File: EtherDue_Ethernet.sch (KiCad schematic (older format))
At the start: 35 parts, among them IC601 W5100, Q601 2N7002, U601 MICROSD, U602 HY931147C, U603 APX811-44UG-7, X601 TXC 7A 25MHz 18pF

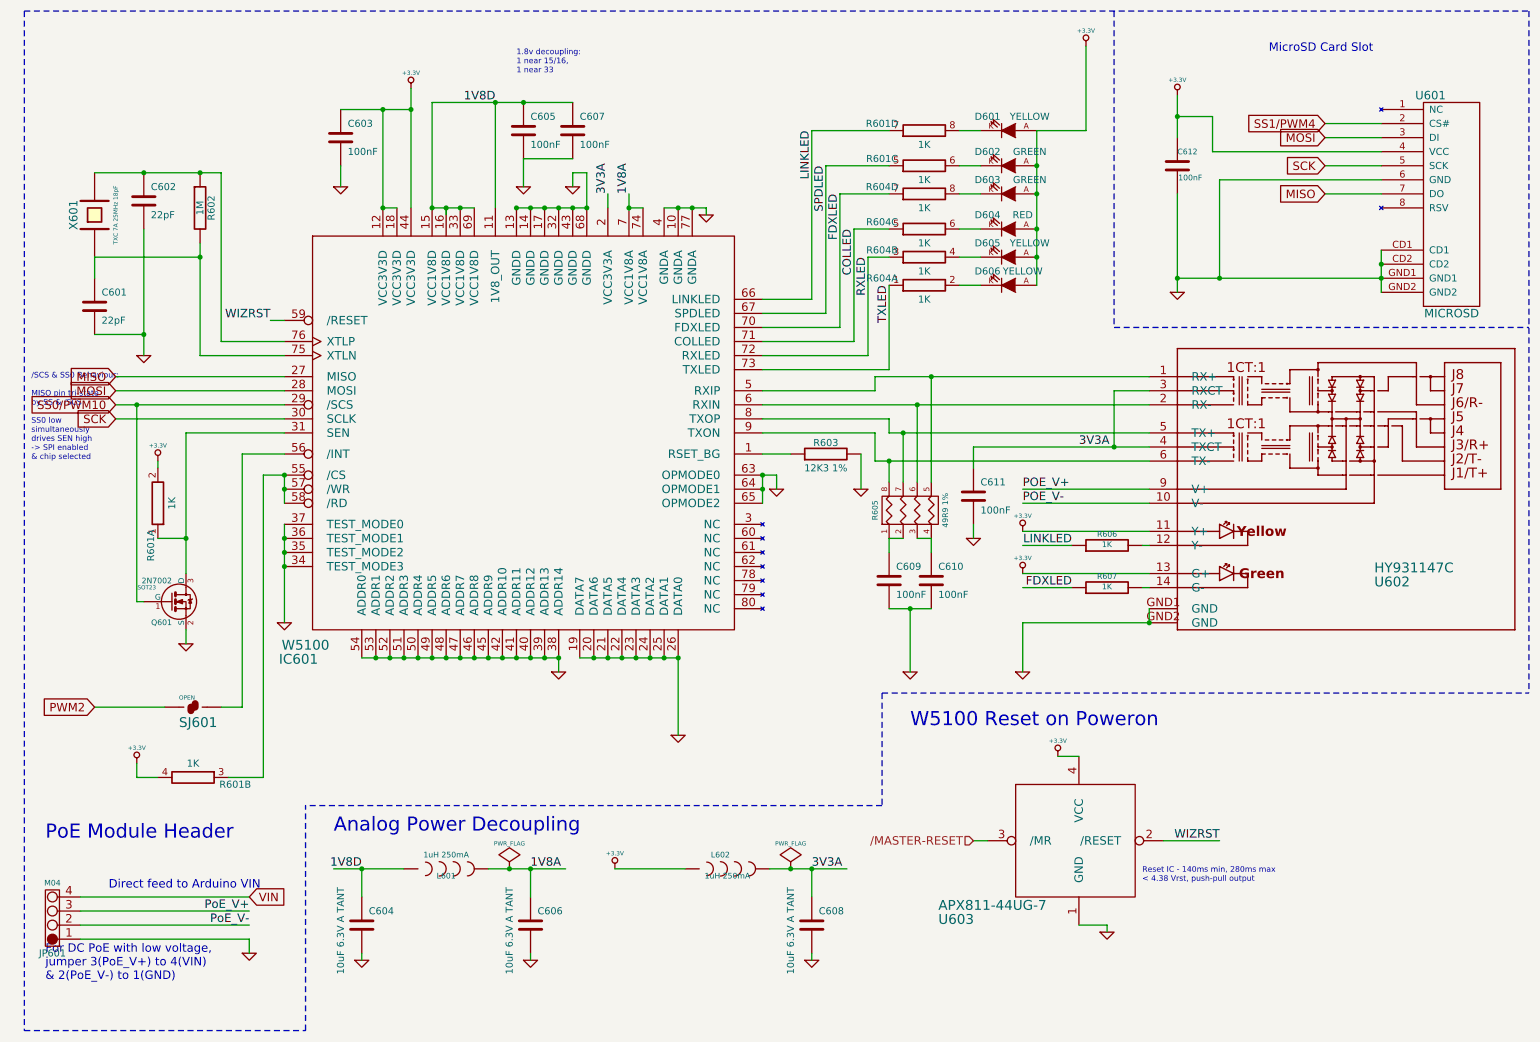
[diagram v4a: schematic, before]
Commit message: Add 24AA025E48 EEPROM w/ unique MAC address
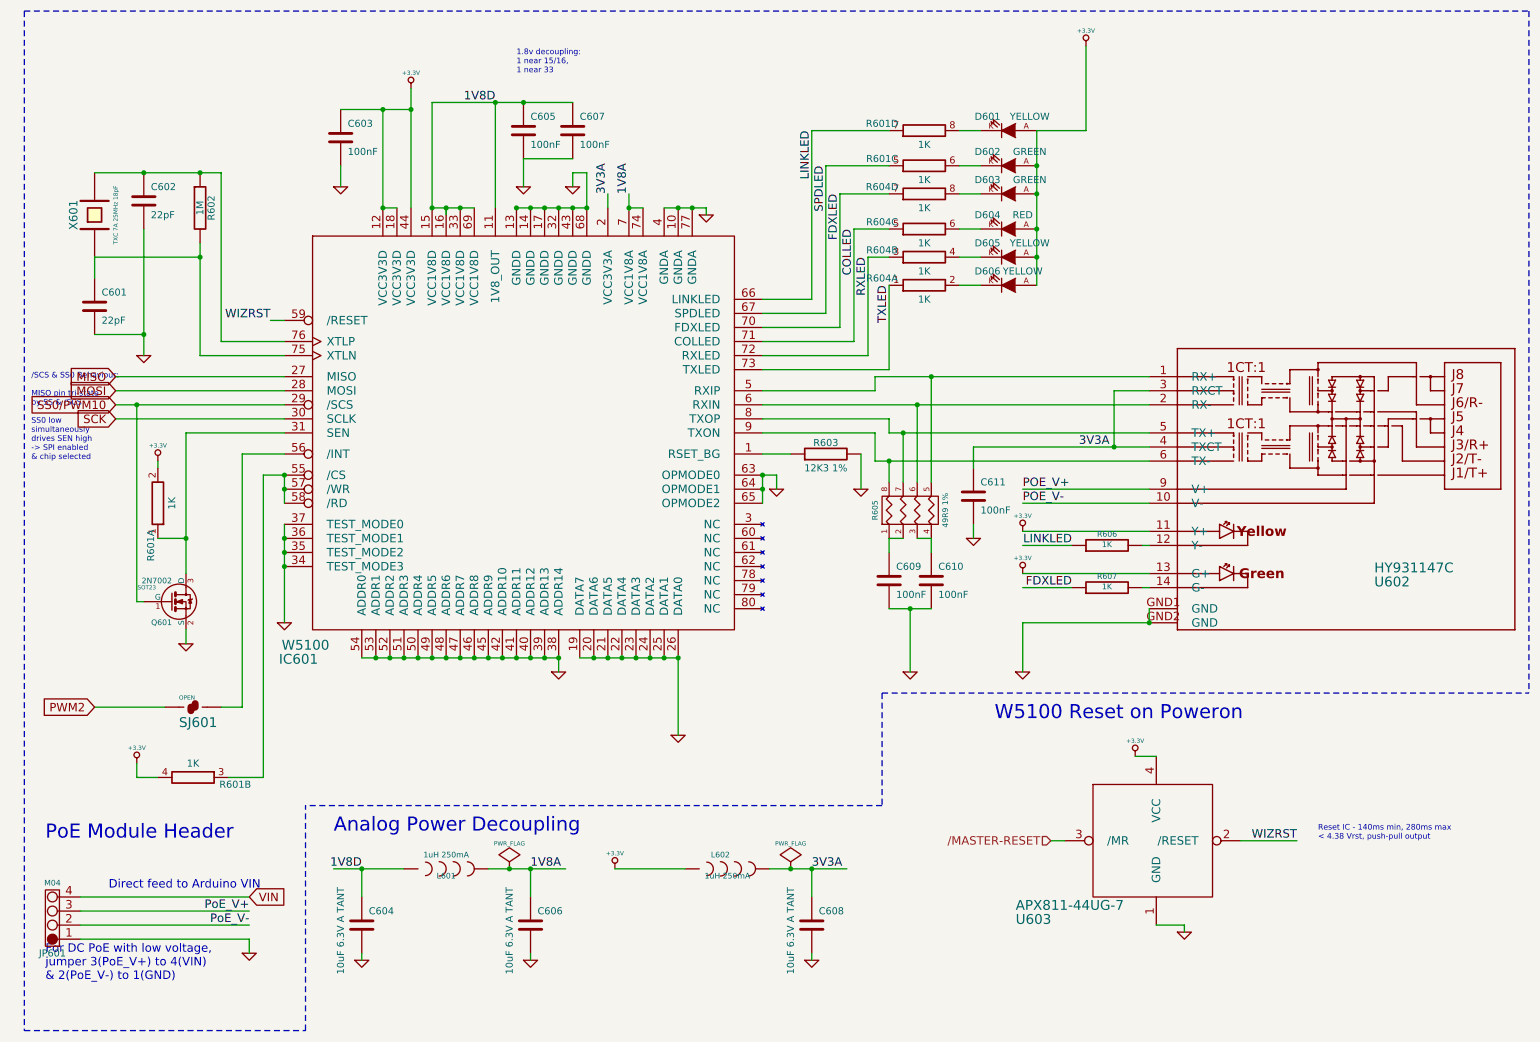
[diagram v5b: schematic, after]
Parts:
- removed C612: 100nF, ~, symbol C
- removed U601: MICROSD, ~, symbol MICROSD
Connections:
- net labels removed: SS1/PWM4
- wire segments 157 -> 144
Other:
- note removed: "MicroSD Card Slot"
- moved on the sheet: U603
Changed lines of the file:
@@
-EESchema Schematic File Version 2  date Fri 28 Jun 2013 16:34:50 EST
+EESchema Schematic File Version 2  date Thu 04 Jul 2013 10:55:52 EST
 LIBS:freetronics_kicad_sch_lib
 LIBS:power
@@
 $Descr A4 11693 8268
 encoding utf-8
-Sheet 6 6
+Sheet 6 7
 Title ""
-Date "27 jun 2013"
+Date "4 jul 2013"
 Rev ""
 Comp ""
@@
 L GND #PWR081
 U 1 1 51663F24
-P 8200 7050
-F 0 "#PWR081" H 8200 7050 30  0001 C CNN
-F 1 "GND" H 8200 6980 30  0001 C CNN
-F 2 "" H 8200 7050 60  0001 C CNN
-F 3 "" H 8200 7050 60  0001 C CNN
-	1    8200 7050
-	1    0    0    -1
-$EndComp
-Wire Wire Line
-	8200 7050 8200 7000
+P 8750 7050
+F 0 "#PWR081" H 8750 7050 30  0001 C CNN
+F 1 "GND" H 8750 6980 30  0001 C CNN
+F 2 "" H 8750 7050 60  0001 C CNN
+F 3 "" H 8750 7050 60  0001 C CNN
+	1    8750 7050
+	1    0    0    -1
+$EndComp
+Wire Wire Line
+	8750 7050 8750 7000
 Wire Wire Line
 	1150 3200 2350 3200
 Wire Wire Line
 	1150 3400 2350 3400
-Wire Wire Line
-	8600 6400 9000 6400
 Wire Notes Line
 	6600 5350 11200 5350
@@
 Connection ~ 6100 6600
 Wire Wire Line
-	7850 5800 8000 5800
-Wire Wire Line
-	7350 6400 7250 6400
+	8400 5800 8550 5800
+Wire Wire Line
+	7900 6400 7800 6400
 Wire Wire Line
 	1150 3300 2350 3300
@@
 Text GLabel 1150 3100 0    60   Input ~ 0
 MISO
-Text HLabel 7250 6400 0    60   Input ~ 0
+Text HLabel 7800 6400 0    60   Input ~ 0
 /MASTER-RESET
-Text Label 9000 6400 2    60   ~ 0
-WIZRST
 $Comp
 L +3.3V #PWR082
 U 1 1 51663BD9
-P 7850 5800
-F 0 "#PWR082" H 7850 5760 30  0001 C CNN
-F 1 "+3.3V" H 7850 5910 30  0000 C CNN
-F 2 "" H 7850 5800 60  0001 C CNN
-F 3 "" H 7850 5800 60  0001 C CNN
-	1    7850 5800
+P 8400 5800
+F 0 "#PWR082" H 8400 5760 30  0001 C CNN
+F 1 "+3.3V" H 8400 5910 30  0000 C CNN
+F 2 "" H 8400 5800 60  0001 C CNN
+F 3 "" H 8400 5800 60  0001 C CNN
+	1    8400 5800
 	1    0    0    -1
 $EndComp
@@
 L APX811 U603
 U 1 1 51663B87
-P 8000 6400
-F 0 "U603" H 7000 5800 70  0000 L BNN
-F 1 "APX811-44UG-7" H 7000 5900 70  0000 L BNN
-F 2 "" H 8000 6400 60  0001 C CNN
-F 3 "" H 8000 6400 60  0001 C CNN
-	1    8000 6400
-	1    0    0    -1
-$EndComp
-Text Notes 6800 5600 0    100  ~ 0
+P 8550 6400
+F 0 "U603" H 7550 5800 70  0000 L BNN
+F 1 "APX811-44UG-7" H 7550 5900 70  0000 L BNN
+F 2 "" H 8550 6400 60  0001 C CNN
+F 3 "" H 8550 6400 60  0001 C CNN
+	1    8550 6400
+	1    0    0    -1
+$EndComp
+Text Notes 7400 5550 0    100  ~ 0
 W5100 Reset on Poweron
 $Comp
@@
 Connection ~ 4000 1900
 Wire Wire Line
-	8200 7000 8000 7000
-Text Notes 8450 6700 0    40   ~ 0
+	8750 7000 8550 7000
+Text Notes 9700 6400 0    40   ~ 0
 Reset IC - 140ms min, 280ms max\n< 4.38 Vrst, push-pull output
 $Comp
@@
 	0    -1   -1   0
 $EndComp
-$Comp
-L MICROSD U601
-U 1 1 51CBA5BE
-P 10600 2000
-F 0 "U601" H 10700 2900 60  0000 C CNN
-F 1 "MICROSD" H 10550 1350 60  0000 C CNN
-F 2 "~" H 10600 2000 60  0000 C CNN
-F 3 "~" H 10600 2000 60  0000 C CNN
-	1    10600 2000
-	-1   0    0    -1
-$EndComp
-$Comp
-L C C612
-U 1 1 51CBA5D2
-P 8700 1600
-F 0 "C612" H 8700 1700 40  0000 L CNN
-F 1 "100nF" H 8706 1515 40  0000 L CNN
-F 2 "~" H 8738 1450 30  0000 C CNN
-F 3 "~" H 8700 1600 60  0000 C CNN
-	1    8700 1600
-	1    0    0    -1
-$EndComp
-$Comp
-L +3.3V #PWR0108
-U 1 1 51CBA5E1
-P 8700 1100
-F 0 "#PWR0108" H 8700 1060 30  0001 C CNN
-F 1 "+3.3V" H 8700 1210 30  0000 C CNN
-F 2 "" H 8700 1100 60  0000 C CNN
-F 3 "" H 8700 1100 60  0000 C CNN
-	1    8700 1100
-	1    0    0    -1
-$EndComp
-Wire Wire Line
-	8700 1400 8700 1100
-Wire Wire Line
-	8950 1500 8950 1250
-Wire Wire Line
-	8950 1250 8700 1250
-Connection ~ 8700 1250
-Wire Wire Line
-	8700 1800 8700 2500
-Wire Wire Line
-	8700 2400 10150 2400
-Wire Wire Line
-	10150 2200 10150 2500
-Connection ~ 10150 2400
-Connection ~ 8700 2400
-$Comp
-L GND #PWR0109
-U 1 1 51CBA9E0
-P 8700 2500
-F 0 "#PWR0109" H 8700 2500 30  0001 C CNN
-F 1 "GND" H 8700 2430 30  0001 C CNN
-F 2 "" H 8700 2500 60  0000 C CNN
-F 3 "" H 8700 2500 60  0000 C CNN
-	1    8700 2500
-	1    0    0    -1
-$EndComp
-Wire Wire Line
-	10150 1300 9750 1300
-Wire Wire Line
-	10150 1400 9750 1400
-Wire Wire Line
-	10150 1600 9750 1600
-Wire Wire Line
-	10150 1800 9750 1800
-Wire Wire Line
-	10150 1500 8950 1500
-Text GLabel 9750 1300 0    60   Input ~ 0
-SS1/PWM4
-Text GLabel 9750 1600 0    60   Input ~ 0
-SCK
-Text GLabel 9750 1400 0    60   Input ~ 0
-MOSI
-Text GLabel 9750 1800 0    60   Input ~ 0
-MISO
-Wire Wire Line
-	10150 1700 9000 1700
-Wire Wire Line
-	9000 1700 9000 2400
-Connection ~ 9000 2400
-Connection ~ 10150 2300
 Wire Wire Line
 	8250 3600 8250 3200
@@
 Wire Wire Line
 	8250 3200 8500 3200
-Wire Notes Line
-	8250 500  8250 2750
-Wire Notes Line
-	8250 2750 11200 2750
-Text Notes 9350 800  0    60   ~ 0
-MicroSD Card Slot
+Text Label 9550 6400 2    60   ~ 0
+WIZRST
+Wire Wire Line
+	9150 6400 9550 6400
 $EndSCHEMATC

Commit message: Update APX811 reset controller for 3.08V threshold
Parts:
- U603: value APX811-44UG-7 -> APX811-31UG-7
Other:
- note added: "Reset IC - 140ms min, 280ms max\n< 3.08 Vrst, push-pull output"
- note removed: "Reset IC - 140ms min, 280ms max\n< 4.38 Vrst, push-pull output"
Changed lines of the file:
@@
 P 8550 6400
 F 0 "U603" H 7550 5800 70  0000 L BNN
-F 1 "APX811-44UG-7" H 7550 5900 70  0000 L BNN
+F 1 "APX811-31UG-7" H 7550 5900 70  0000 L BNN
 F 2 "" H 8550 6400 60  0001 C CNN
 F 3 "" H 8550 6400 60  0001 C CNN
@@
 	8750 7000 8550 7000
 Text Notes 9700 6400 0    40   ~ 0
-Reset IC - 140ms min, 280ms max\n< 4.38 Vrst, push-pull output
+Reset IC - 140ms min, 280ms max\n< 3.08 Vrst, push-pull output
 $Comp
 L SJ SJ601
